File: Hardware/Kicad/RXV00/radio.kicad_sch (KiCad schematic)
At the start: 17 parts, among them J2 U.FL, U3 SX1281IMLTRT, Y2 52MHz 8pF

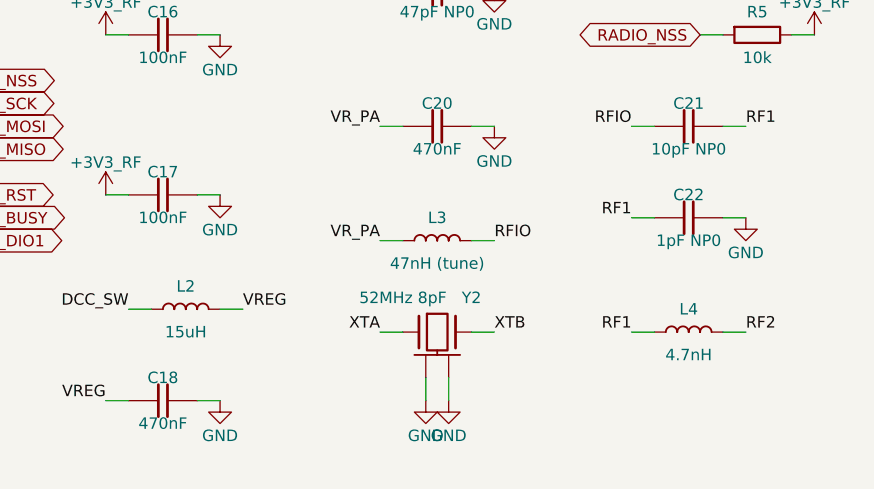
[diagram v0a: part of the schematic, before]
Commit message: Upgrade to KiCad 10 and use shared Kicad_Libs only
- Upgrade ESCV00, FCV00, RXV00, VTXV00 schematics and PCBs to KiCad 10
- Remove KiCad_Libs_Drone and merge_libs (parts already in Kicad_Libs)
- Lib tables list every Kicad_Libs library
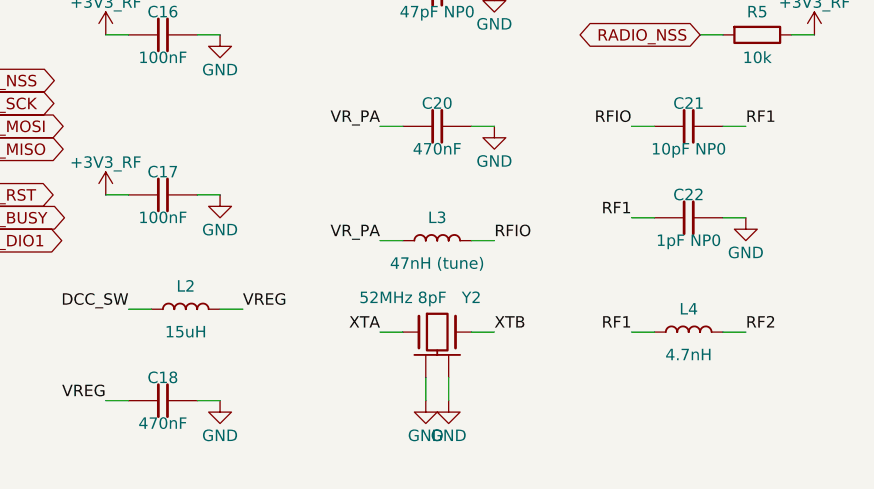
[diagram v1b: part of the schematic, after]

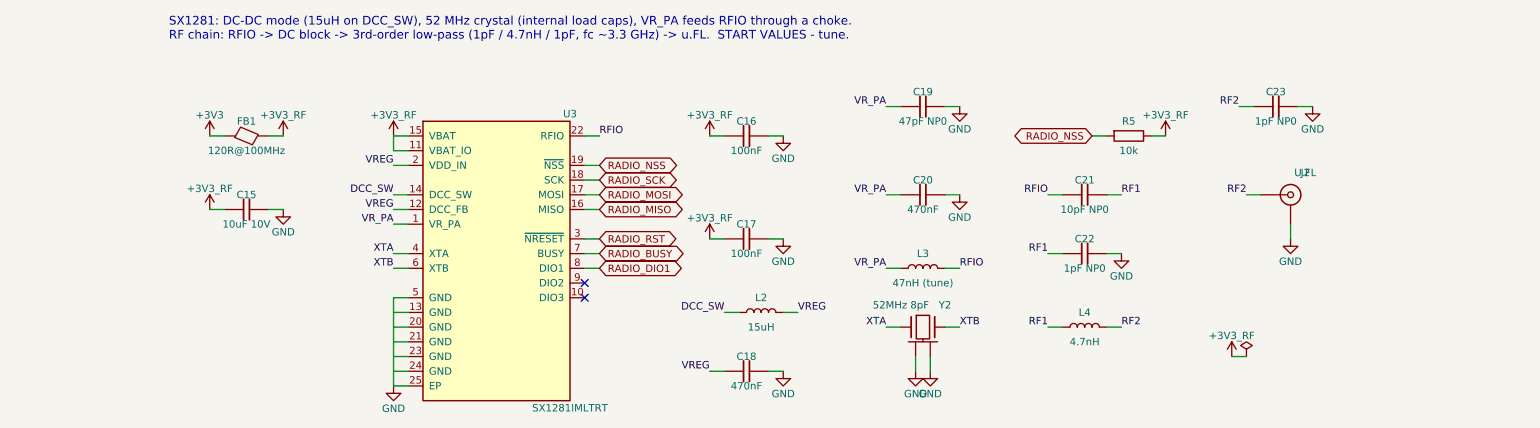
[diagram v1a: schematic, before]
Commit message: Boards follow the B0_EE part convention
- every real part uses the symbol/footprint/3D/datasheet named after its MPN in Kicad_Libs
- symbols keep only Reference, Value, Footprint, Datasheet, Description
  (MPN, Manufacturer, Verify, LCSC, Note fields removed; Verify notes moved to the Readme)
- schematic symbol caches rebuilt from the libraries, PCB footprints relinked with the
  same fields and 3D models as the library (connectivity unchanged)
- DNP and BOM attributes of the footprints match the symbols
- BOMs re-exported with kicad-cli
- ignore KiCad local history
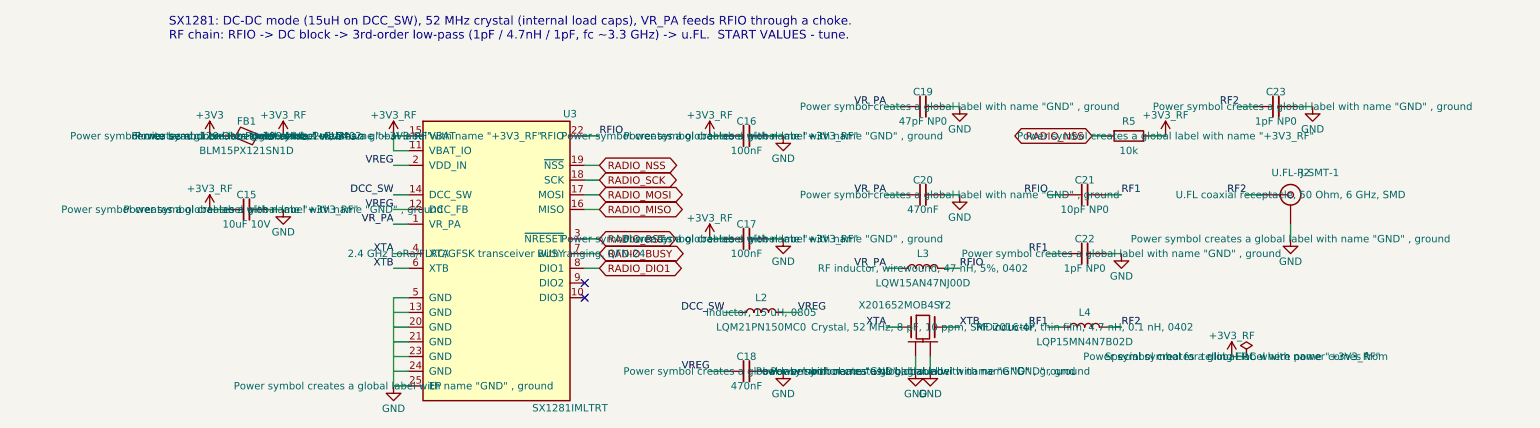
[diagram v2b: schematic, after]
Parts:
- FB1: value 120R@100MHz -> BLM15PX121SN1D; footprint eChoke:L_0402_1005Metric -> eFerrite:BLM15PX121SN1D; symbol eChoke:FB -> eFerrite:BLM15PX121SN1D; MPN BLM15PX121SN1D -> (none)
- J2: value U.FL -> U.FL-R-SMT-1; footprint eConnector:U.FL_Hirose_U.FL-R-SMT-1_Vertical -> eConnector:U.FL-R-SMT-1; symbol eConnector:Conn_Coaxial -> eConnector:U.FL-R-SMT-1; MPN U.FL-R-SMT-1(10) -> (none); Manufacturer Hirose -> (none)
- L2: value 15uH -> LQM21PN150MC0; footprint eCoil:L_0805_2012Metric -> eCoil:LQM21PN150MC0; symbol eCoil:L -> eCoil:LQM21PN150MC0; MPN LQM21PN150MC0 -> (none); Manufacturer Murata -> (none)
- L3: value 47nH (tune) -> LQW15AN47NJ00D; footprint eCoil:L_0402_1005Metric -> eCoil:LQW15AN47NJ00D; symbol eCoil:L -> eCoil:LQW15AN47NJ00D; MPN LQW15AN47NJ00 -> (none); Manufacturer Murata -> (none)
- L4: value 4.7nH -> LQP15MN4N7B02D; footprint eCoil:L_0402_1005Metric -> eCoil:LQP15MN4N7B02D; symbol eCoil:L -> eCoil:LQP15MN4N7B02D; MPN LQP15MN4N7B02 -> (none); Manufacturer Murata -> (none)
- U3: footprint eRFModule:QFN-24-1EP_4x4mm_P0.5mm_EP2.6x2.6mm -> eRFModule:SX1281IMLTRT; MPN SX1281IMLTRT -> (none); Manufacturer Semtech -> (none); Verify Pin table typed from Semtech DS_SX1280-1 rev 3.x. RF matchi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 -> (none)
- Y2: value 52MHz 8pF -> X201652MOB4SI; footprint eCrystal:Crystal_SMD_2016-4Pin_2.0x1.6mm -> eCrystal:X201652MOB4SI; symbol eCrystal:Crystal_GND24 -> eCrystal:X201652MOB4SI; MPN X201652MOB4SI -> (none); Manufacturer Yangxing -> (none); Note SX1280 reference: 52 MHz, +/-10ppm -> (none)

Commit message: Cleared all the descriptions and started Power section for FCV
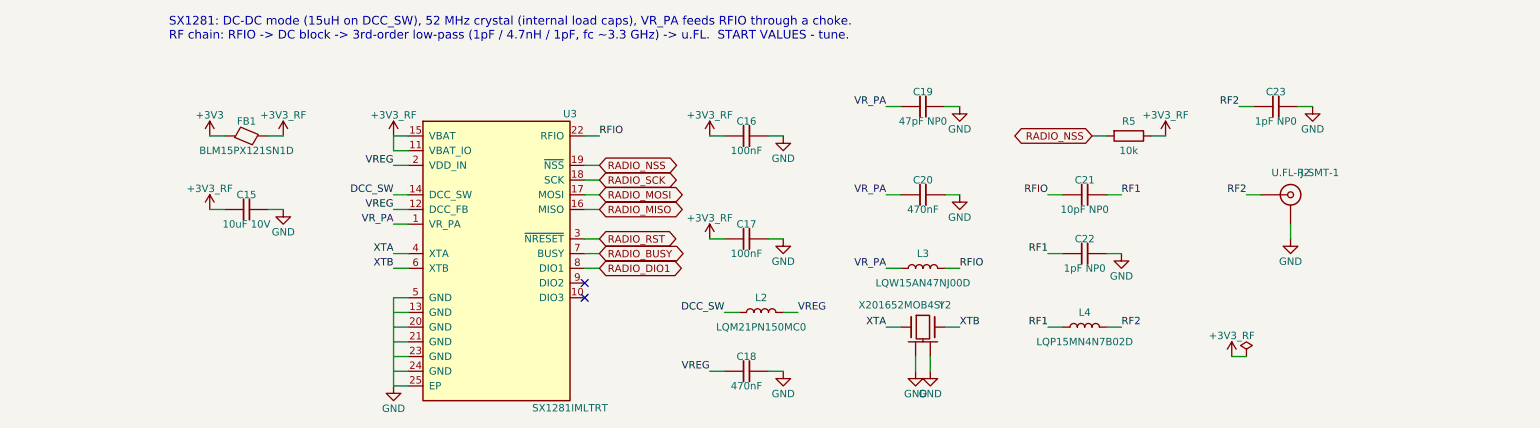
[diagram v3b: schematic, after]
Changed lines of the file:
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@@
 			(show_name no)
 			(do_not_autoplace no)
+			(hide yes)
 			(effects
 				(font
@@
 			(show_name no)
 			(do_not_autoplace no)
+			(hide yes)
 			(effects
 				(font
@@
 			(show_name no)
 			(do_not_autoplace no)
+			(hide yes)
 			(effects
 				(font
@@
 			(show_name no)
 			(do_not_autoplace no)
+			(hide yes)
 			(effects
 				(font
@@
 			(show_name no)
 			(do_not_autoplace no)
+			(hide yes)
 			(effects
 				(font
@@
 			(show_name no)
 			(do_not_autoplace no)
+			(hide yes)
 			(effects
 				(font
@@
 			(show_name no)
 			(do_not_autoplace no)
+			(hide yes)
 			(effects
 				(font
@@
 			(show_name no)
 			(do_not_autoplace no)
+			(hide yes)
 			(effects
 				(font
@@
 			(show_name no)
 			(do_not_autoplace no)
+			(hide yes)
 			(effects
 				(font
@@
 			(show_name no)
 			(do_not_autoplace no)
+			(hide yes)
 			(effects
 				(font
@@
 			(show_name no)
 			(do_not_autoplace no)
+			(hide yes)
 			(effects
 				(font
@@
 			(show_name no)
 			(do_not_autoplace no)
+			(hide yes)
 			(effects
 				(font
@@
 			(show_name no)
 			(do_not_autoplace no)
+			(hide yes)
 			(effects
 				(font
@@
 			(show_name no)
 			(do_not_autoplace no)
+			(hide yes)
 			(effects
 				(font
@@
 			(show_name no)
 			(do_not_autoplace no)
+			(hide yes)
 			(effects
 				(font
@@
 			(show_name no)
 			(do_not_autoplace no)
+			(hide yes)
 			(effects
 				(font
@@
 			(show_name no)
 			(do_not_autoplace no)
+			(hide yes)
 			(effects
 				(font
@@
 			(show_name no)
 			(do_not_autoplace no)
+			(hide yes)
 			(effects
 				(font
@@
 			(show_name no)
 			(do_not_autoplace no)
+			(hide yes)
 			(effects
 				(font
@@
 			(show_name no)
 			(do_not_autoplace no)
+			(hide yes)
 			(effects
 				(font
@@
 			(show_name no)
 			(do_not_autoplace no)
+			(hide yes)
 			(effects
 				(font
@@
 			(show_name no)
 			(do_not_autoplace no)
+			(hide yes)
 			(effects
 				(font
@@
 			(show_name no)
 			(do_not_autoplace no)
+			(hide yes)
 			(effects
 				(font
@@
 			(show_name no)
 			(do_not_autoplace no)
+			(hide yes)
 			(effects
 				(font
@@
 			(show_name no)
 			(do_not_autoplace no)
+			(hide yes)
 			(effects
 				(font
@@
 			(show_name no)
 			(do_not_autoplace no)
+			(hide yes)
 			(effects
 				(font
@@
 			(show_name no)
 			(do_not_autoplace no)
+			(hide yes)
 			(effects
 				(font
@@
 			(show_name no)
 			(do_not_autoplace no)
-			(effects
-				(font
+			(hide yes)
+			(effects
+				(font
